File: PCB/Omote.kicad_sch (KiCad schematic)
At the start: 172 parts, among them J1 USB_C_Receptacle_USB2.0, J2 Conn_01x50, J3 JST_PH_B2B-PH, J4 2.54x2 Header, J5 Micro_SD_Card, Q1 DMG2301L, Q2 MBT3904DW1, Q3 DMG2301L, Q4 DMG2301L, Q5 DMG2301L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

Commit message: Fixed LCSC number for R7/R9
The LCSC part number  for R7 and R9 was wrongly linked to a 5.1 Ohm resistor instead of a 5.1 KiloOhm resistor.
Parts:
- R7, R9: LCSC C114626 -> C105580
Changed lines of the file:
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@@
 			)
 		)
-		(property "LCSC" "C114626"
+		(property "LCSC" "C105580"
 			(at 69.85 66.04 0)
 			(effects
@@
 			)
 		)
-		(property "LCSC" "C114626"
+		(property "LCSC" "C105580"
 			(at 60.96 66.04 0)
 			(effects

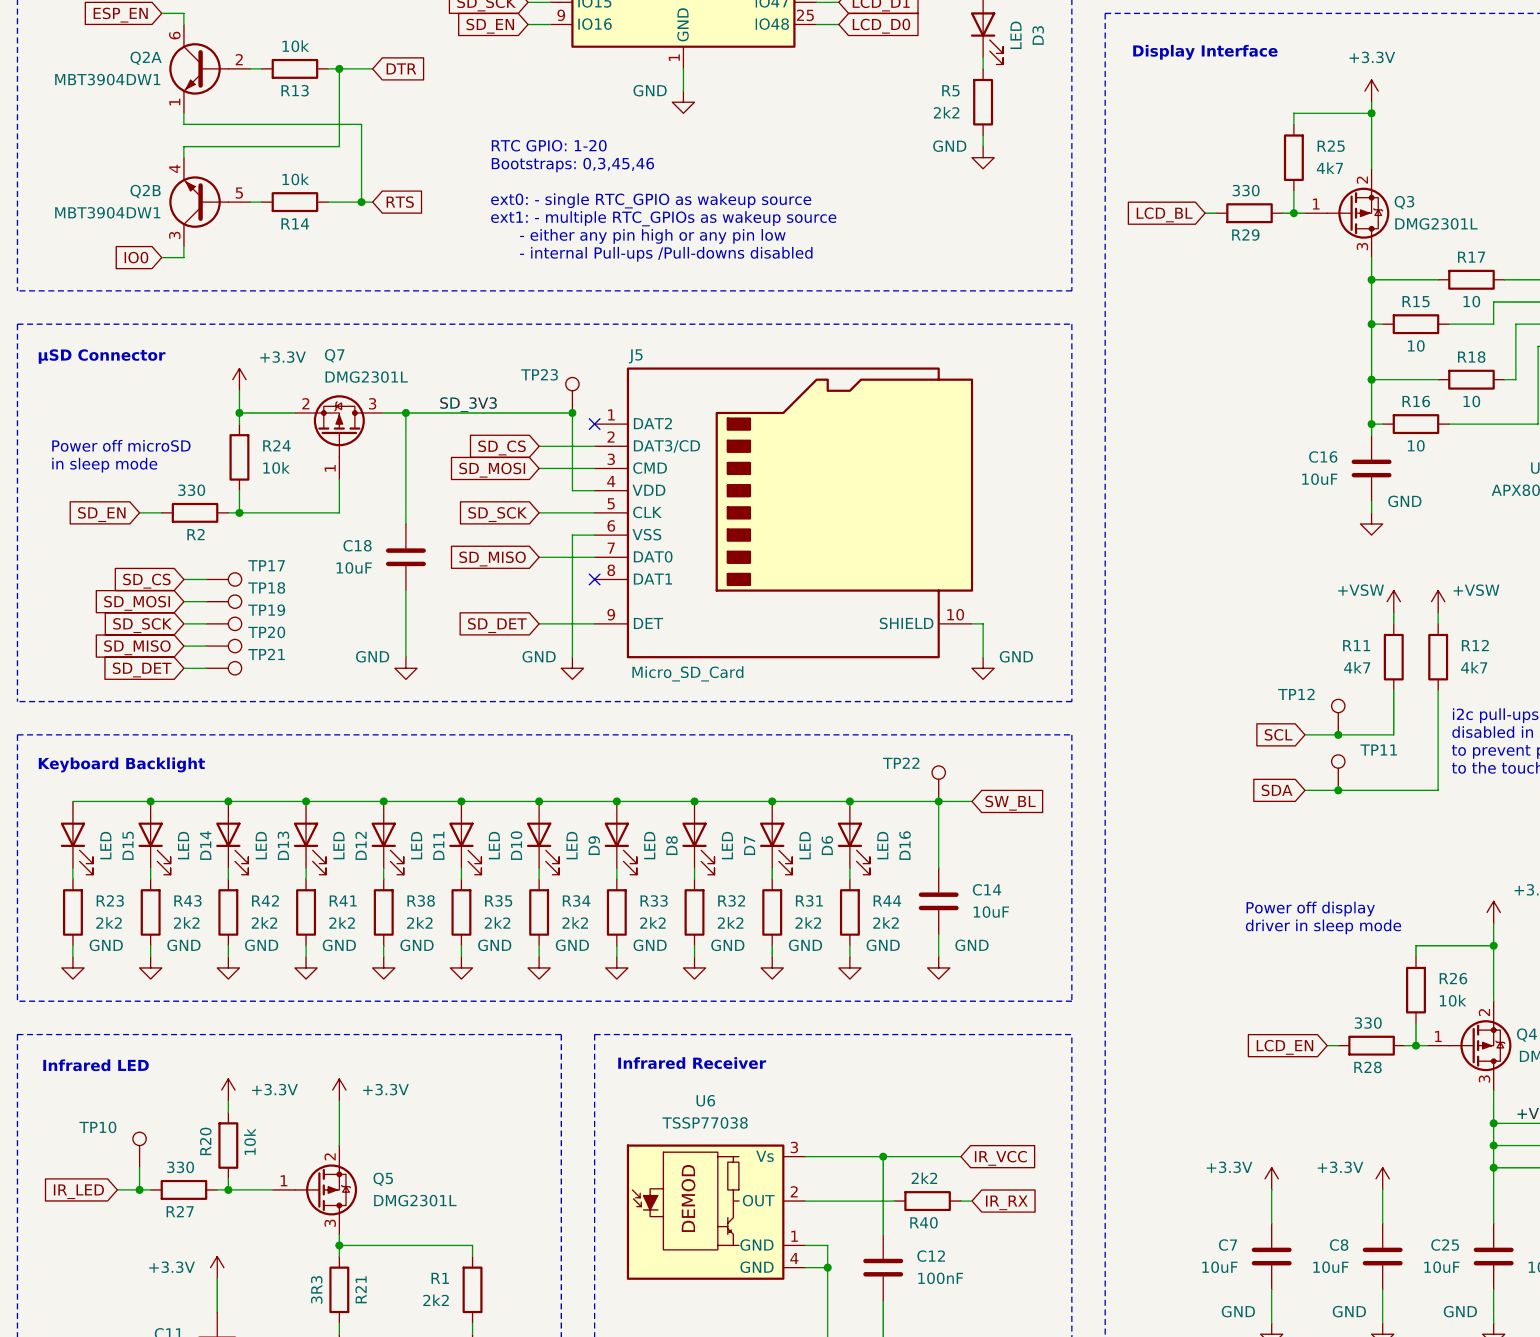
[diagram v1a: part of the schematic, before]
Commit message: MOSFET circuit adjustment
- Increased gate resistors from 330Ohm to 1kOhm to lower edge speeds slightly (not absolutely necessary but 1k seems to be a default value for most display eval boards)
- Set R25 (gate pull-up for backlight) to 10kOhm like all others
- Removed C14 to reduce load on the ESP32 pin
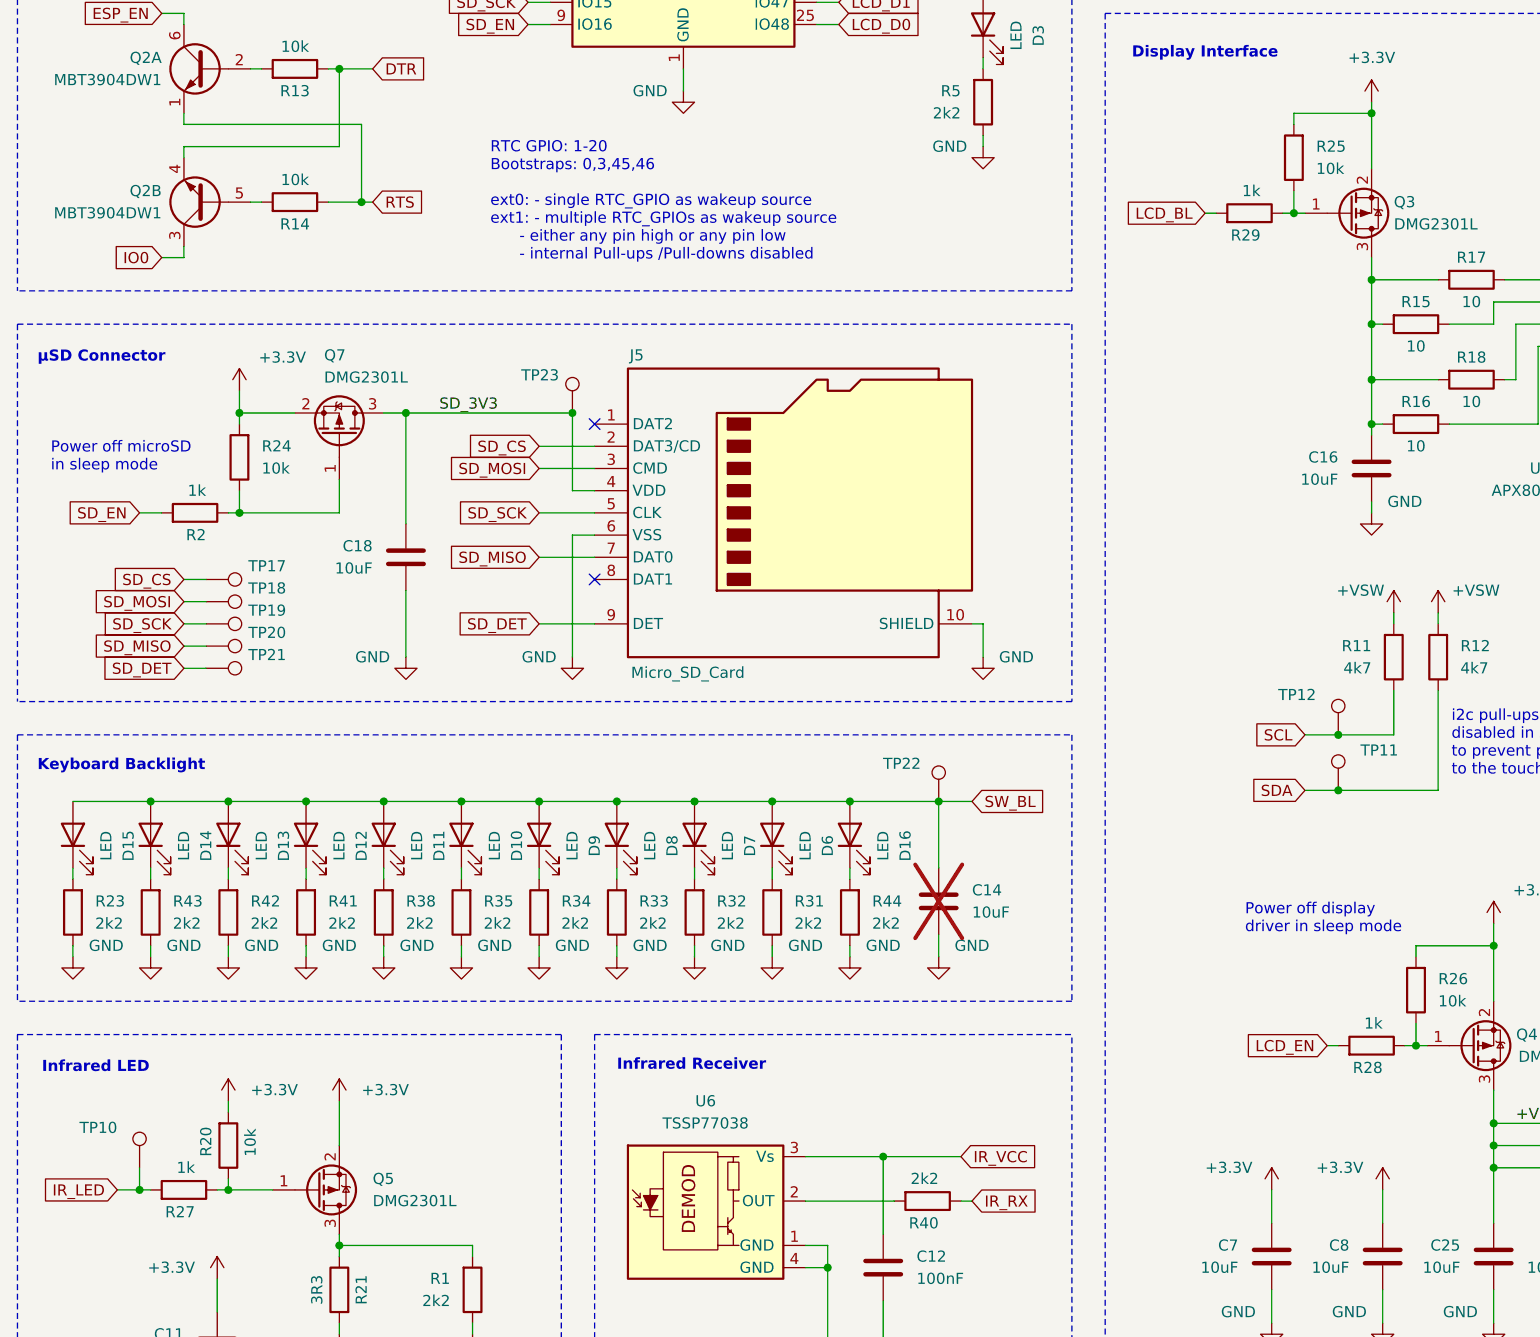
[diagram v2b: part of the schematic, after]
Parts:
- C14: now not fitted; now left out of the parts list
- R2, R27, R28, R29: value 330 -> 1k; LCSC C105881 -> C22548
- R25: value 4k7 -> 10k; LCSC C99782 -> C98220
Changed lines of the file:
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@@
 		(unit 1)
 		(exclude_from_sim no)
-		(in_bom yes)
+		(in_bom no)
 		(on_board yes)
-		(dnp no)
+		(dnp yes)
 		(property "Reference" "C14"
 			(at 281.94 180.3399 0)
@@
 			)
 		)
-		(property "Value" "4k7"
+		(property "Value" "10k"
 			(at 321.31 97.7899 0)
 			(effects
@@
 			)
 		)
-		(property "LCSC" "C99782"
+		(property "LCSC" "C98220"
 			(at 318.77 96.52 0)
 			(effects
@@
 			)
 		)
-		(property "Value" "330"
+		(property "Value" "1k"
 			(at 314.96 100.33 90)
 			(effects
@@
 			)
 		)
-		(property "LCSC" "C105881"
+		(property "LCSC" "C22548"
 			(at 313.69 102.87 0)
 			(effects
@@
 			)
 		)
-		(property "Value" "330"
+		(property "Value" "1k"
 			(at 193.04 212.09 90)
 			(effects
@@
 			)
 		)
-		(property "LCSC" "C105881"
+		(property "LCSC" "C22548"
 			(at 191.77 214.63 0)
 			(effects
@@
 			)
 		)
-		(property "Value" "330"
+		(property "Value" "1k"
 			(at 328.93 195.58 90)
 			(effects
@@
 			)
 		)
-		(property "LCSC" "C105881"
+		(property "LCSC" "C22548"
 			(at 327.66 198.12 0)
 			(effects
@@
 			)
 		)
-		(property "Value" "330"
+		(property "Value" "1k"
 			(at 194.31 134.62 90)
 			(effects
@@
 			)
 		)
-		(property "LCSC" "C105881"
+		(property "LCSC" "C22548"
 			(at 193.04 137.16 0)
 			(effects
